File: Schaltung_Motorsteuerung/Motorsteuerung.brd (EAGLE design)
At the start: 100 x 64.8 mm, 22 parts, among them IC1 ULN2003AN, IC2 LM324P, X1 22-23-2021, X2 22-23-2021, X3 22-23-2021, X5 22-23-2021

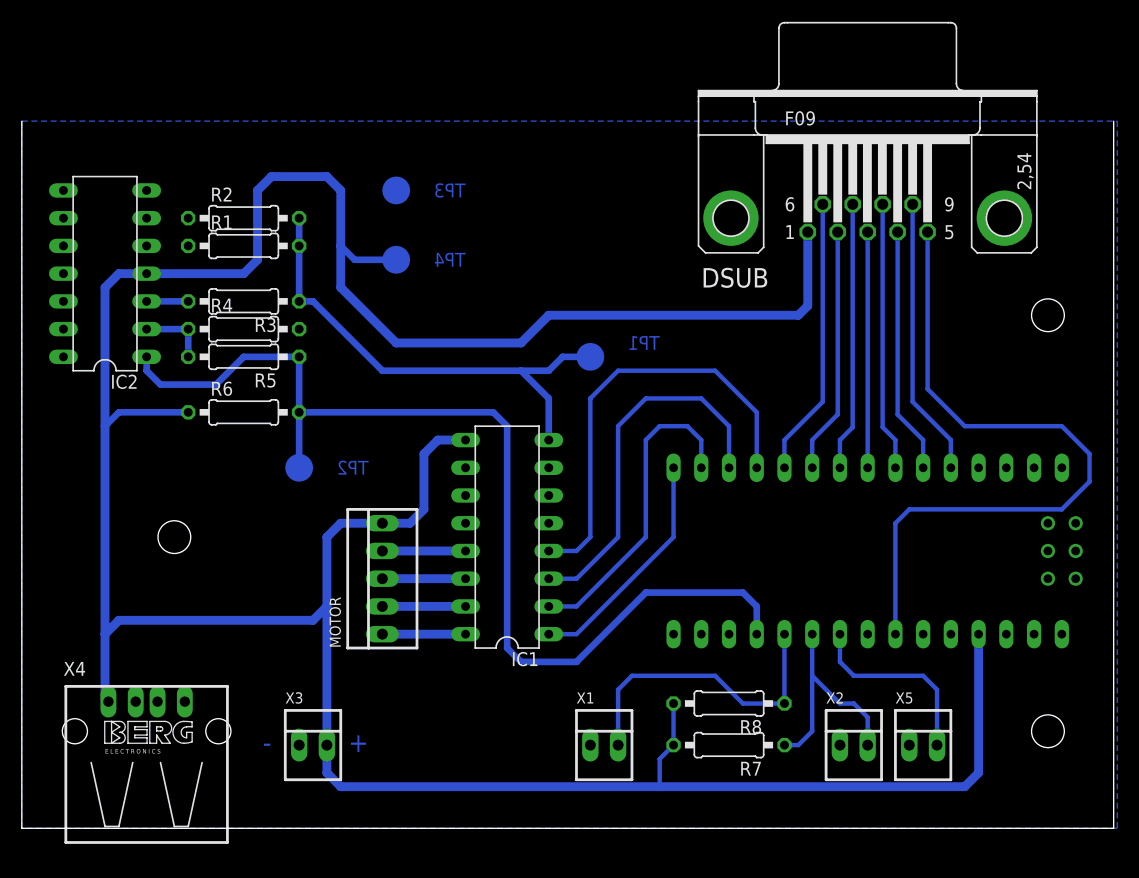
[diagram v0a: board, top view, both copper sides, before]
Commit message: Update 5
added Bib-Library, Casings an many new parts to the documentation
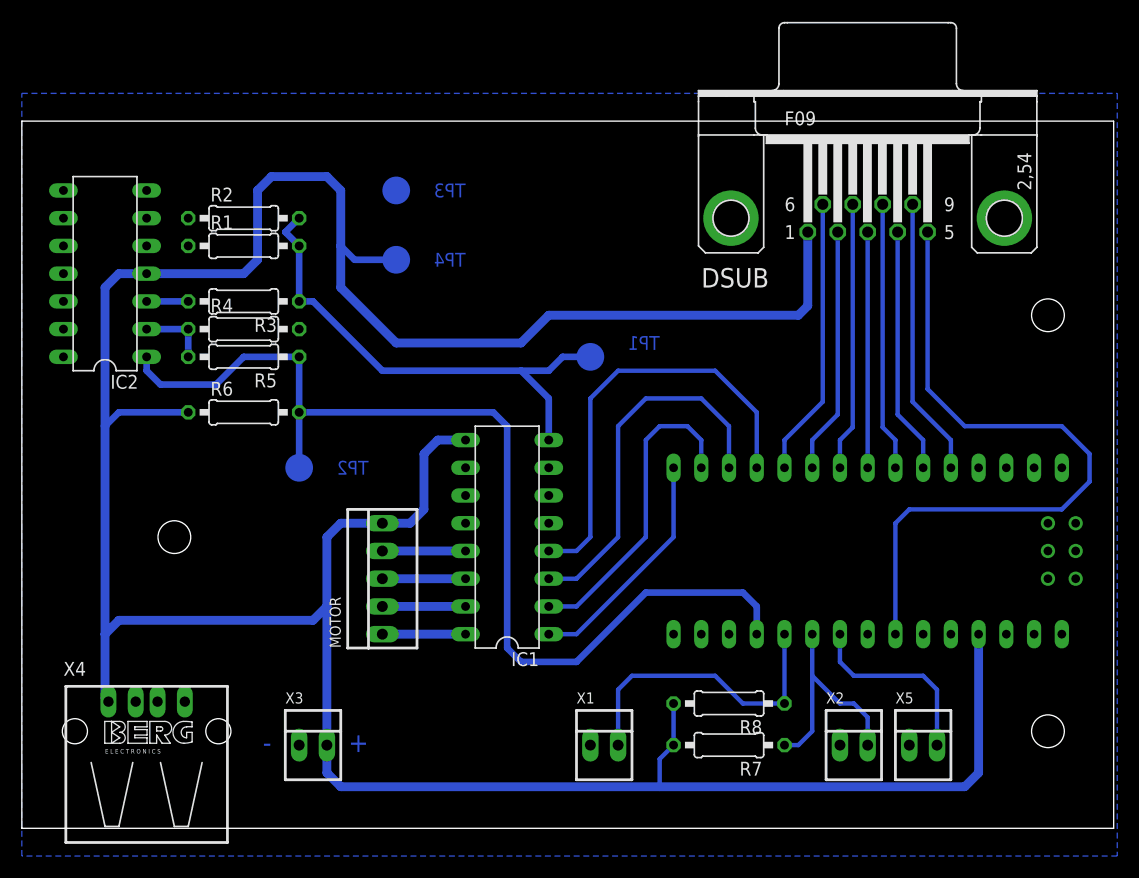
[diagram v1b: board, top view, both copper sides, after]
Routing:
- net N$9: track 44.8 -> 45.9 mm
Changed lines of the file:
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@@
 <wire x1="100" y1="15.24" x2="100" y2="80" width="0" layer="20"/>
 <wire x1="0" y1="80" x2="0" y2="15.24" width="0" layer="20"/>
-<dimension x1="0" y1="80.01" x2="100.33" y2="80.01" x3="50.165" y3="80.01" textsize="1.778" layer="16"/>
 <hole x="13.97" y="41.91" drill="3"/>
 <hole x="93.98" y="24.13" drill="3"/>
@@
 <text x="31.75" y="22.225" size="1.778" layer="16" font="vector" rot="MR0">+</text>
 <text x="22.86" y="22.225" size="1.778" layer="16" font="vector" rot="MR0">-</text>
-<dimension x1="-1.27" y1="80.01" x2="-1.27" y2="15.24" x3="-2.54" y3="47.625" textsize="1.778" layer="16"/>
+<wire x1="0" y1="80.01" x2="100" y2="80.01" width="0" layer="20"/>
 </plain>
 <attributes>
@@
 <contactref element="X5" pad="1"/>
 <polygon width="0.2" layer="16" isolate="0.35">
-<vertex x="0" y="80.01"/>
-<vertex x="100.33" y="80.01"/>
-<vertex x="100.33" y="15.24"/>
-<vertex x="0" y="15.24"/>
+<vertex x="0" y="82.55"/>
+<vertex x="100.33" y="82.55"/>
+<vertex x="100.33" y="12.7"/>
+<vertex x="0" y="12.7"/>
 </polygon>
 <contactref element="U$1" pad="GND1"/>
@@
 <contactref element="R1" pad="2"/>
 <wire x1="25.4" y1="68.58" x2="25.4" y2="63.5" width="0.6096" layer="16"/>
-<wire x1="25.4" y1="71.12" x2="25.4" y2="68.58" width="0.6096" layer="16"/>
+<wire x1="25.4" y1="71.12" x2="24.13" y2="69.85" width="0.6096" layer="16"/>
+<wire x1="24.13" y1="69.85" x2="25.4" y2="68.58" width="0.6096" layer="16"/>
 <wire x1="48.26" y1="54.61" x2="45.72" y2="57.15" width="0.6096" layer="16"/>
 <wire x1="48.26" y1="54.61" x2="48.26" y2="50.8" width="0.6096" layer="16"/>
